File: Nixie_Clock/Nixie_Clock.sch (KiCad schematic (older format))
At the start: 1 part

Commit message: Completed Nixie Page
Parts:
- removed U?: SAML21E15B-M, Housings_DFN_QFN:QFN-32-1EP_5x5mm_Pitch0.5mm, symbol SAML21E15B-M
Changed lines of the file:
@@
 LIBS:contrib
 LIBS:valves
+LIBS:nixie_tubes
+LIBS:nixie_clock
+LIBS:Nixie_Clock-cache
 EELAYER 25 0
 EELAYER END
 $Descr A4 11693 8268
 encoding utf-8
-Sheet 1 1
+Sheet 1 4
 Title ""
 Date ""
@@
 Comment4 ""
 $EndDescr
-$Comp
-L SAML21E15B-M U?
-U 1 1 59B58923
-P 4500 3100
-F 0 "U?" H 2400 4500 50  0000 C CNN
-F 1 "SAML21E15B-M" H 6300 1700 50  0000 C CNN
-F 2 "Housings_DFN_QFN:QFN-32-1EP_5x5mm_Pitch0.5mm" H 4500 2100 50  0001 C CIN
-F 3 "" H 4500 3100 50  0000 C CNN
-	1    4500 3100
-	1    0    0    -1
-$EndComp
+$Sheet
+S 4000 1500 1600 2800
+U 59B58CCA
+F0 "uController" 60
+F1 "nixie_clk_ucontroller.sch" 60
+$EndSheet
+$Sheet
+S 1300 1250 1600 1300
+U 59B58C72
+F0 "Power" 60
+F1 "nixie_clk_power.sch" 60
+$EndSheet
+$Sheet
+S 6050 1200 950  3100
+U 59B58C95
+F0 "Nixie Tubes" 60
+F1 "nixie_clk_tubes.sch" 60
+F2 "PP180V" I L 6050 1400 60
+F3 "GK1" I L 6050 1650 60
+F4 "GK2" I L 6050 1800 60
+F5 "GK3" I L 6050 1950 60
+F6 "GK4" I L 6050 2100 60
+F7 "GK5" I L 6050 2250 60
+F8 "GK6" I L 6050 2400 60
+F9 "GK7" I L 6050 2550 60
+F10 "GK8" I L 6050 2700 60
+F11 "GK9" I L 6050 2850 60
+F12 "GK0" I L 6050 3000 60
+F13 "KC" I L 6050 3150 60
+F14 "GA1" I L 6050 3400 60
+F15 "GA2" I L 6050 3550 60
+F16 "GA3" I L 6050 3700 60
+F17 "GA4" I L 6050 3850 60
+F18 "GA5" I L 6050 4000 60
+F19 "GA6" I L 6050 4150 60
+$EndSheet
 $EndSCHEMATC

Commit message: Almost done with uC page
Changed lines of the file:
@@
 F0 "uController" 60
 F1 "nixie_clk_ucontroller.sch" 60
+F2 "TC0WO0" I R 5600 1650 60
+F3 "TC0WO1" I R 5600 1800 60
+F4 "TC1WO0" I R 5600 1950 60
+F5 "TC1WO1" I R 5600 2100 60
+F6 "TC3WO0" I R 5600 2250 60
+F7 "TC3WO1" I R 5600 2400 60
+F8 "TC2WO0" I R 5600 2550 60
+F9 "TC2WO1" I R 5600 2700 60
+F10 "TC4WO0" I R 5600 2850 60
+F11 "TC4WO1" I R 5600 3000 60
+F12 "TC5WO0" I R 5600 3150 60
+F13 "PA08" I R 5600 3400 60
+F14 "PA09" I R 5600 3550 60
+F15 "PA10" I R 5600 3700 60
+F16 "PA11" I R 5600 3850 60
+F17 "PA25" I R 5600 4000 60
+F18 "PA27" I R 5600 4150 60
+F19 "PA28" I L 4000 4100 60
 $EndSheet
 $Sheet
@@
 F0 "Nixie Tubes" 60
 F1 "nixie_clk_tubes.sch" 60
-F2 "PP180V" I L 6050 1400 60
+F2 "PP180V" I L 6050 1300 60
 F3 "GK1" I L 6050 1650 60
 F4 "GK2" I L 6050 1800 60
@@
 F19 "GA6" I L 6050 4150 60
 $EndSheet
+Wire Wire Line
+	5600 1650 6050 1650
+Wire Wire Line
+	5600 1800 6050 1800
+Wire Wire Line
+	5600 1950 6050 1950
+Wire Wire Line
+	5600 2100 6050 2100
+Wire Wire Line
+	5600 2250 6050 2250
+Wire Wire Line
+	5600 2400 6050 2400
+Wire Wire Line
+	5600 2550 6050 2550
+Wire Wire Line
+	5600 2700 6050 2700
+Wire Wire Line
+	5600 2850 6050 2850
+Wire Wire Line
+	5600 3000 6050 3000
+Wire Wire Line
+	5600 3150 6050 3150
+Wire Wire Line
+	5600 3400 6050 3400
+Wire Wire Line
+	5600 3550 6050 3550
+Wire Wire Line
+	5600 3700 6050 3700
+Wire Wire Line
+	5600 3850 6050 3850
+Wire Wire Line
+	5600 4000 6050 4000
+Wire Wire Line
+	5600 4150 6050 4150
 $EndSCHEMATC

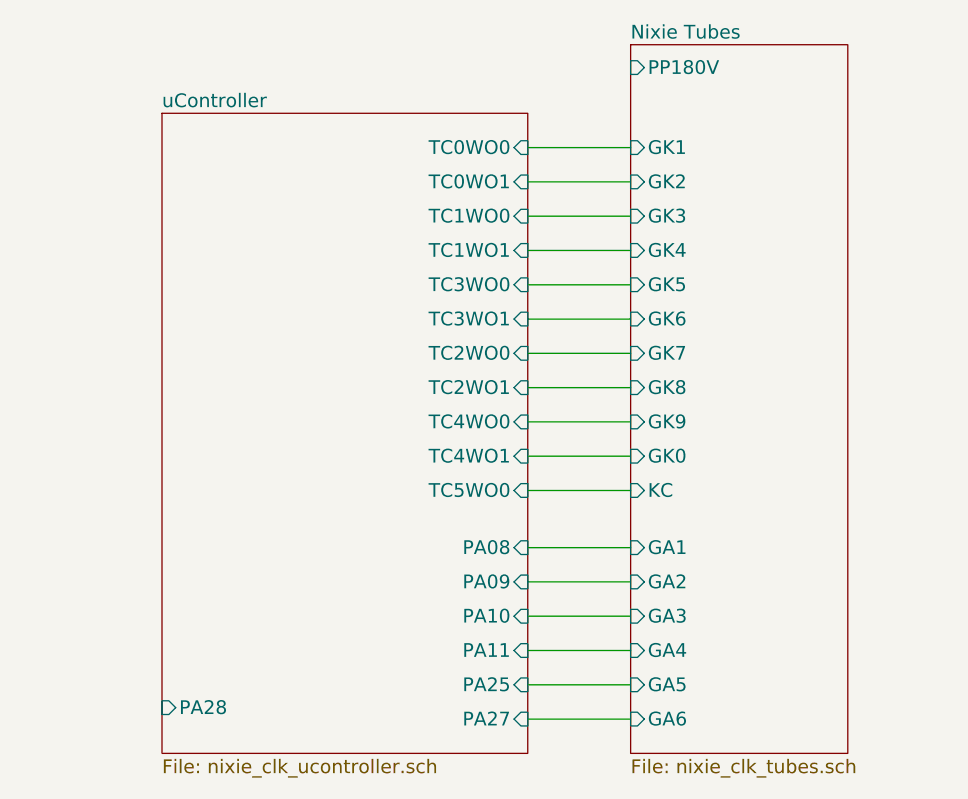
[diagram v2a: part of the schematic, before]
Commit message: Added HV5122 and RaspPi
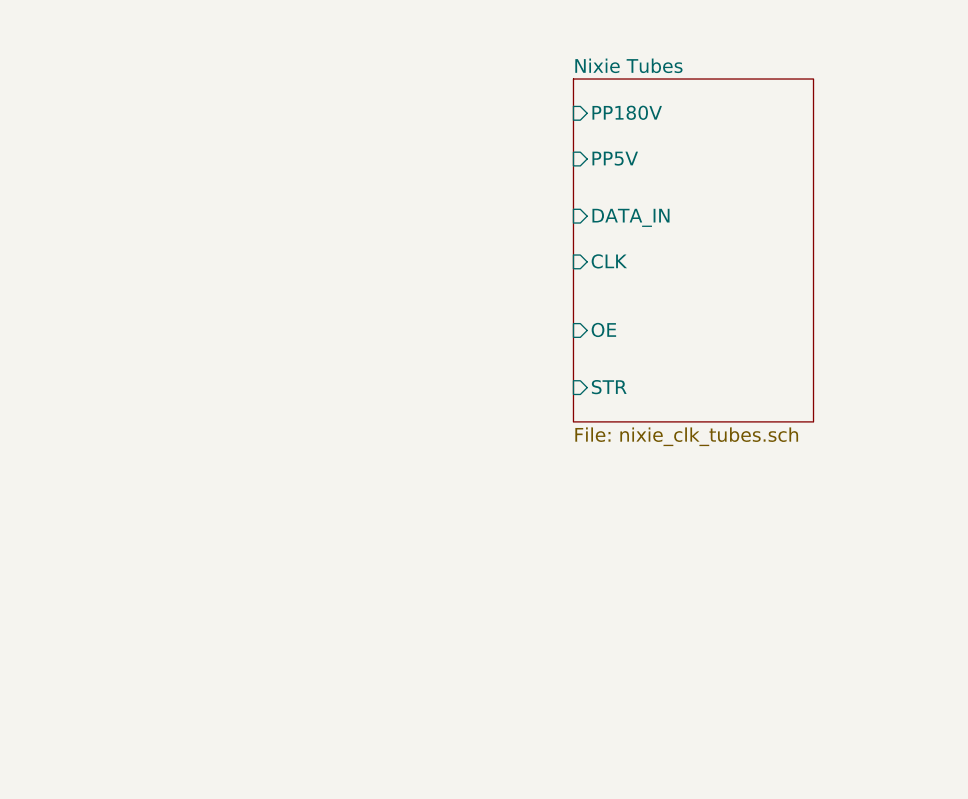
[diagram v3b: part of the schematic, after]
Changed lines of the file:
@@
 $Descr A4 11693 8268
 encoding utf-8
-Sheet 1 4
+Sheet 1 3
 Title ""
 Date ""
@@
 $EndDescr
 $Sheet
-S 4000 1500 1600 2800
-U 59B58CCA
-F0 "uController" 60
-F1 "nixie_clk_ucontroller.sch" 60
-F2 "TC0WO0" I R 5600 1650 60
-F3 "TC0WO1" I R 5600 1800 60
-F4 "TC1WO0" I R 5600 1950 60
-F5 "TC1WO1" I R 5600 2100 60
-F6 "TC3WO0" I R 5600 2250 60
-F7 "TC3WO1" I R 5600 2400 60
-F8 "TC2WO0" I R 5600 2550 60
-F9 "TC2WO1" I R 5600 2700 60
-F10 "TC4WO0" I R 5600 2850 60
-F11 "TC4WO1" I R 5600 3000 60
-F12 "TC5WO0" I R 5600 3150 60
-F13 "PA08" I R 5600 3400 60
-F14 "PA09" I R 5600 3550 60
-F15 "PA10" I R 5600 3700 60
-F16 "PA11" I R 5600 3850 60
-F17 "PA25" I R 5600 4000 60
-F18 "PA27" I R 5600 4150 60
-F19 "PA28" I L 4000 4100 60
-$EndSheet
-$Sheet
 S 1300 1250 1600 1300
 U 59B58C72
@@
 $EndSheet
 $Sheet
-S 6050 1200 950  3100
+S 5800 1350 1050 1500
 U 59B58C95
 F0 "Nixie Tubes" 60
 F1 "nixie_clk_tubes.sch" 60
-F2 "PP180V" I L 6050 1300 60
-F3 "GK1" I L 6050 1650 60
-F4 "GK2" I L 6050 1800 60
-F5 "GK3" I L 6050 1950 60
-F6 "GK4" I L 6050 2100 60
-F7 "GK5" I L 6050 2250 60
-F8 "GK6" I L 6050 2400 60
-F9 "GK7" I L 6050 2550 60
-F10 "GK8" I L 6050 2700 60
-F11 "GK9" I L 6050 2850 60
-F12 "GK0" I L 6050 3000 60
-F13 "KC" I L 6050 3150 60
-F14 "GA1" I L 6050 3400 60
-F15 "GA2" I L 6050 3550 60
-F16 "GA3" I L 6050 3700 60
-F17 "GA4" I L 6050 3850 60
-F18 "GA5" I L 6050 4000 60
-F19 "GA6" I L 6050 4150 60
+F2 "PP5V" I L 5800 1700 60
+F3 "DATA_IN" I L 5800 1950 60
+F4 "CLK" I L 5800 2150 60
+F5 "OE" I L 5800 2450 60
+F6 "STR" I L 5800 2700 60
+F7 "PP180V" I L 5800 1500 60
 $EndSheet
-Wire Wire Line
-	5600 1650 6050 1650
-Wire Wire Line
-	5600 1800 6050 1800
-Wire Wire Line
-	5600 1950 6050 1950
-Wire Wire Line
-	5600 2100 6050 2100
-Wire Wire Line
-	5600 2250 6050 2250
-Wire Wire Line
-	5600 2400 6050 2400
-Wire Wire Line
-	5600 2550 6050 2550
-Wire Wire Line
-	5600 2700 6050 2700
-Wire Wire Line
-	5600 2850 6050 2850
-Wire Wire Line
-	5600 3000 6050 3000
-Wire Wire Line
-	5600 3150 6050 3150
-Wire Wire Line
-	5600 3400 6050 3400
-Wire Wire Line
-	5600 3550 6050 3550
-Wire Wire Line
-	5600 3700 6050 3700
-Wire Wire Line
-	5600 3850 6050 3850
-Wire Wire Line
-	5600 4000 6050 4000
-Wire Wire Line
-	5600 4150 6050 4150
 $EndSCHEMATC

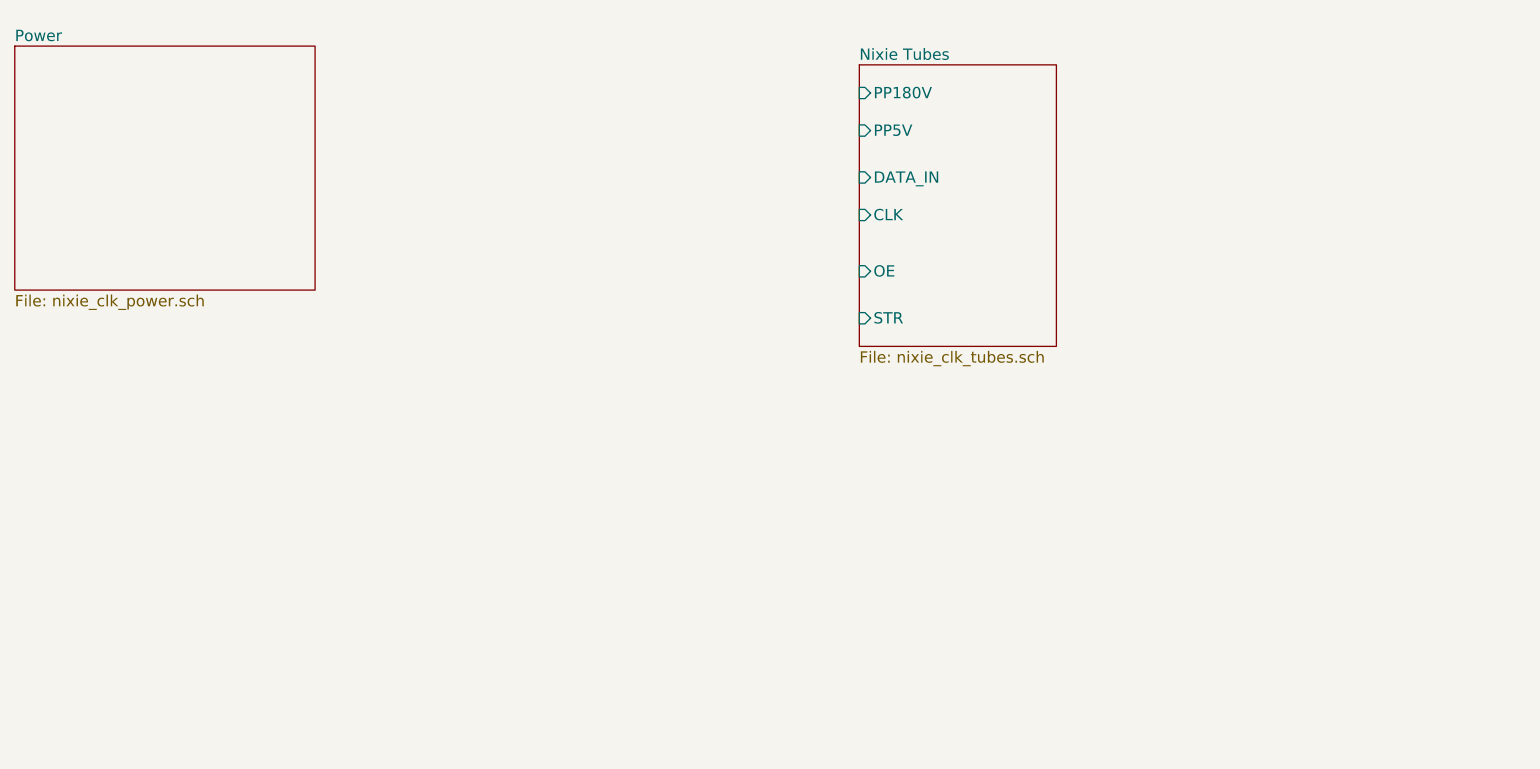
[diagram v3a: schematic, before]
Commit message: Added controller and initial release for 5V AC-DC converter
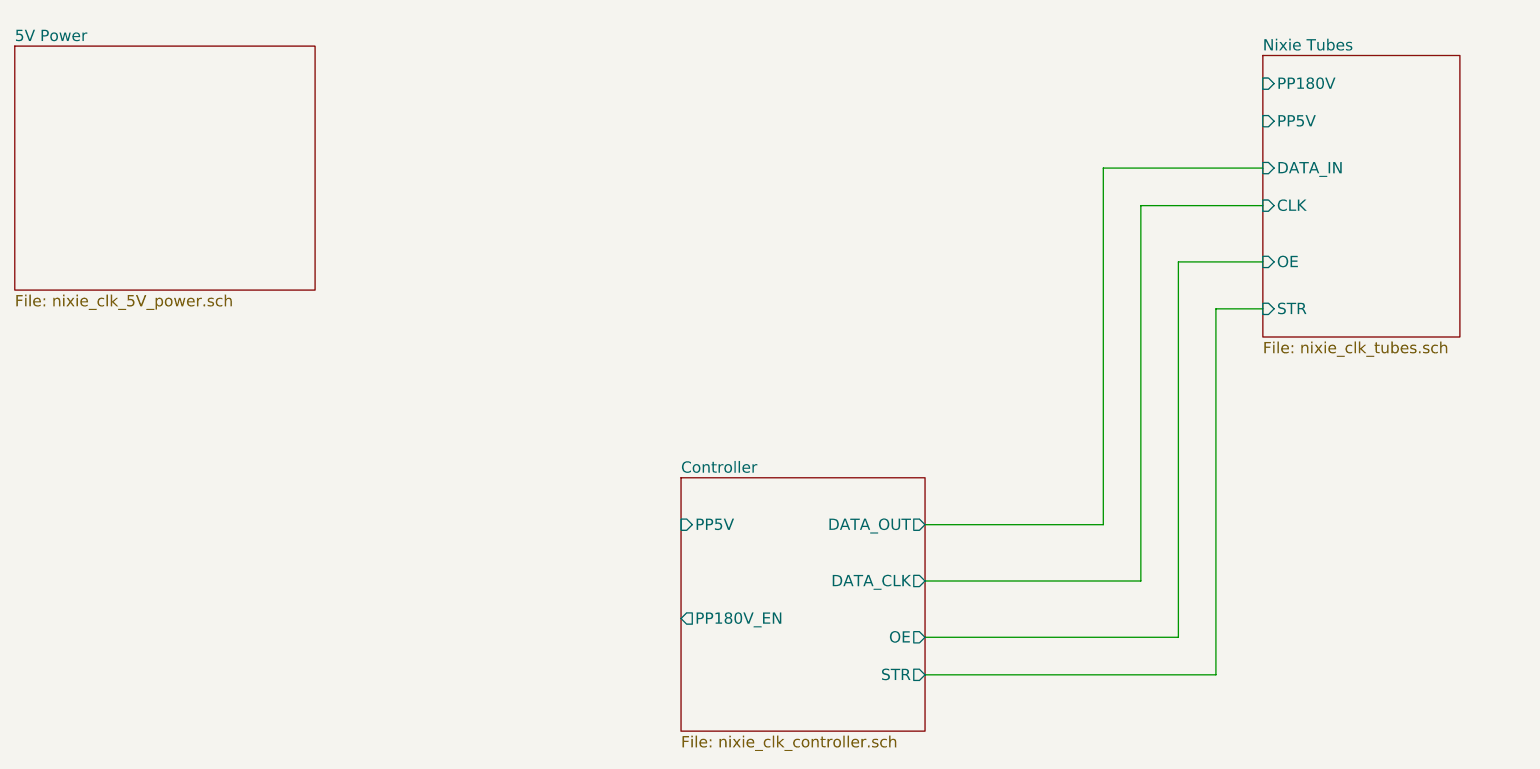
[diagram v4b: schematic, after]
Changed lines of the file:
@@
 $Descr A4 11693 8268
 encoding utf-8
-Sheet 1 3
+Sheet 1 4
 Title ""
 Date ""
@@
 S 1300 1250 1600 1300
 U 59B58C72
-F0 "Power" 60
-F1 "nixie_clk_power.sch" 60
+F0 "5V Power" 60
+F1 "nixie_clk_5V_power.sch" 60
 $EndSheet
 $Sheet
-S 5800 1350 1050 1500
+S 7950 1300 1050 1500
 U 59B58C95
 F0 "Nixie Tubes" 60
 F1 "nixie_clk_tubes.sch" 60
-F2 "PP5V" I L 5800 1700 60
-F3 "DATA_IN" I L 5800 1950 60
-F4 "CLK" I L 5800 2150 60
-F5 "OE" I L 5800 2450 60
-F6 "STR" I L 5800 2700 60
-F7 "PP180V" I L 5800 1500 60
+F2 "PP5V" I L 7950 1650 60
+F3 "DATA_IN" I L 7950 1900 60
+F4 "CLK" I L 7950 2100 60
+F5 "OE" I L 7950 2400 60
+F6 "STR" I L 7950 2650 60
+F7 "PP180V" I L 7950 1450 60
 $EndSheet
+$Sheet
+S 4850 3550 1300 1350
+U 59D05E9F
+F0 "Controller" 60
+F1 "nixie_clk_controller.sch" 60
+F2 "DATA_OUT" O R 6150 3800 60
+F3 "DATA_CLK" O R 6150 4100 60
+F4 "PP5V" I L 4850 3800 60
+F5 "PP180V_EN" O L 4850 4300 60
+F6 "STR" O R 6150 4600 60
+F7 "OE" O R 6150 4400 60
+$EndSheet
+Wire Wire Line
+	6150 3800 7100 3800
+Wire Wire Line
+	7100 3800 7100 1900
+Wire Wire Line
+	7100 1900 7950 1900
+Wire Wire Line
+	6150 4100 7300 4100
+Wire Wire Line
+	7300 4100 7300 2100
+Wire Wire Line
+	7300 2100 7950 2100
+Wire Wire Line
+	6150 4400 7500 4400
+Wire Wire Line
+	7500 4400 7500 2400
+Wire Wire Line
+	7500 2400 7950 2400
+Wire Wire Line
+	6150 4600 7700 4600
+Wire Wire Line
+	7700 4600 7700 2650
+Wire Wire Line
+	7700 2650 7950 2650
 $EndSCHEMATC
